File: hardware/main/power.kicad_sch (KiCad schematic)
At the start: 5 parts

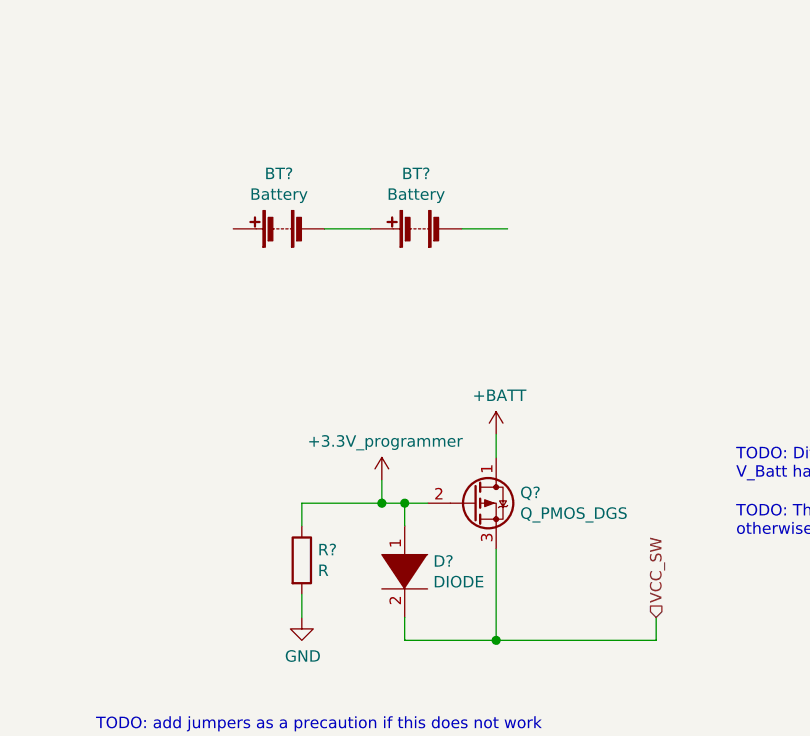
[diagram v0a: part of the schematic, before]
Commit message: Add new board outline
Reason: This makes the first design iteration of the case possible.
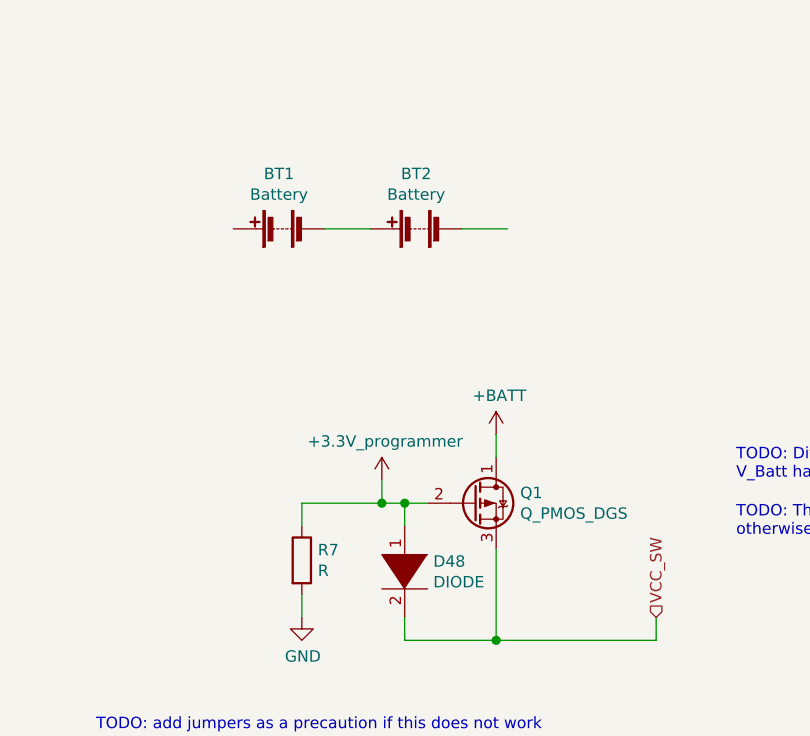
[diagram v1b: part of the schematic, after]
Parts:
- gave numbers to parts that had none: 5
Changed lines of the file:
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@@
   (symbol (lib_id "power:+5V") (at 40.64 34.29 0) (unit 1)
     (in_bom yes) (on_board yes)
-    (property "Reference" "#PWR?" (id 0) (at 40.64 38.1 0)
+    (property "Reference" "#PWR0127" (id 0) (at 40.64 38.1 0)
       (effects (font (size 1.27 1.27)) hide)
     )
@@
   (symbol (lib_id "power:+3.3V") (at 81.28 121.92 0) (unit 1)
     (in_bom yes) (on_board yes)
-    (property "Reference" "#PWR?" (id 0) (at 81.28 125.73 0)
+    (property "Reference" "#PWR0126" (id 0) (at 81.28 125.73 0)
       (effects (font (size 1.27 1.27)) hide)
     )
@@
   (symbol (lib_id "power:+BATT") (at 93.98 116.84 0) (unit 1)
     (in_bom yes) (on_board yes)
-    (property "Reference" "#PWR?" (id 0) (at 93.98 120.65 0)
+    (property "Reference" "#PWR0125" (id 0) (at 93.98 120.65 0)
       (effects (font (size 1.27 1.27)) hide)
     )
@@
   (symbol (lib_id "power:GND") (at 72.39 137.16 0) (unit 1)
     (in_bom yes) (on_board yes)
-    (property "Reference" "#PWR?" (id 0) (at 72.39 143.51 0)
+    (property "Reference" "#PWR0128" (id 0) (at 72.39 143.51 0)
       (effects (font (size 1.27 1.27)) hide)
     )
@@
   (symbol (lib_id "Device:R") (at 72.39 130.81 0) (unit 1)
     (in_bom yes) (on_board yes)
-    (property "Reference" "R?" (id 0) (at 74.1681 129.6606 0)
+    (property "Reference" "R7" (id 0) (at 74.1681 129.6606 0)
       (effects (font (size 1.27 1.27)) (justify left))
     )
@@
   (symbol (lib_id "Device:Battery") (at 69.85 93.98 90) (unit 1)
     (in_bom yes) (on_board yes)
-    (property "Reference" "BT?" (id 0) (at 69.85 87.8648 90))
+    (property "Reference" "BT1" (id 0) (at 69.85 87.8648 90))
     (property "Value" "Battery" (id 1) (at 69.85 90.1635 90))
     (property "Footprint" "" (id 2) (at 68.326 93.98 90)
@@
   (symbol (lib_id "Device:Battery") (at 85.09 93.98 90) (unit 1)
     (in_bom yes) (on_board yes)
-    (property "Reference" "BT?" (id 0) (at 85.09 87.8648 90))
+    (property "Reference" "BT2" (id 0) (at 85.09 87.8648 90))
     (property "Value" "Battery" (id 1) (at 85.09 90.1635 90))
     (property "Footprint" "" (id 2) (at 83.566 93.98 90)
@@
   (symbol (lib_id "pspice:DIODE") (at 83.82 132.08 270) (unit 1)
     (in_bom yes) (on_board yes)
-    (property "Reference" "D?" (id 0) (at 86.9951 130.9306 90)
+    (property "Reference" "D48" (id 0) (at 86.9951 130.9306 90)
       (effects (font (size 1.27 1.27)) (justify left))
     )
@@
   (symbol (lib_id "Device:Q_PMOS_DGS") (at 91.44 124.46 0) (unit 1)
     (in_bom yes) (on_board yes)
-    (property "Reference" "Q?" (id 0) (at 96.6471 123.3106 0)
+    (property "Reference" "Q1" (id 0) (at 96.6471 123.3106 0)
       (effects (font (size 1.27 1.27)) (justify left))
     )

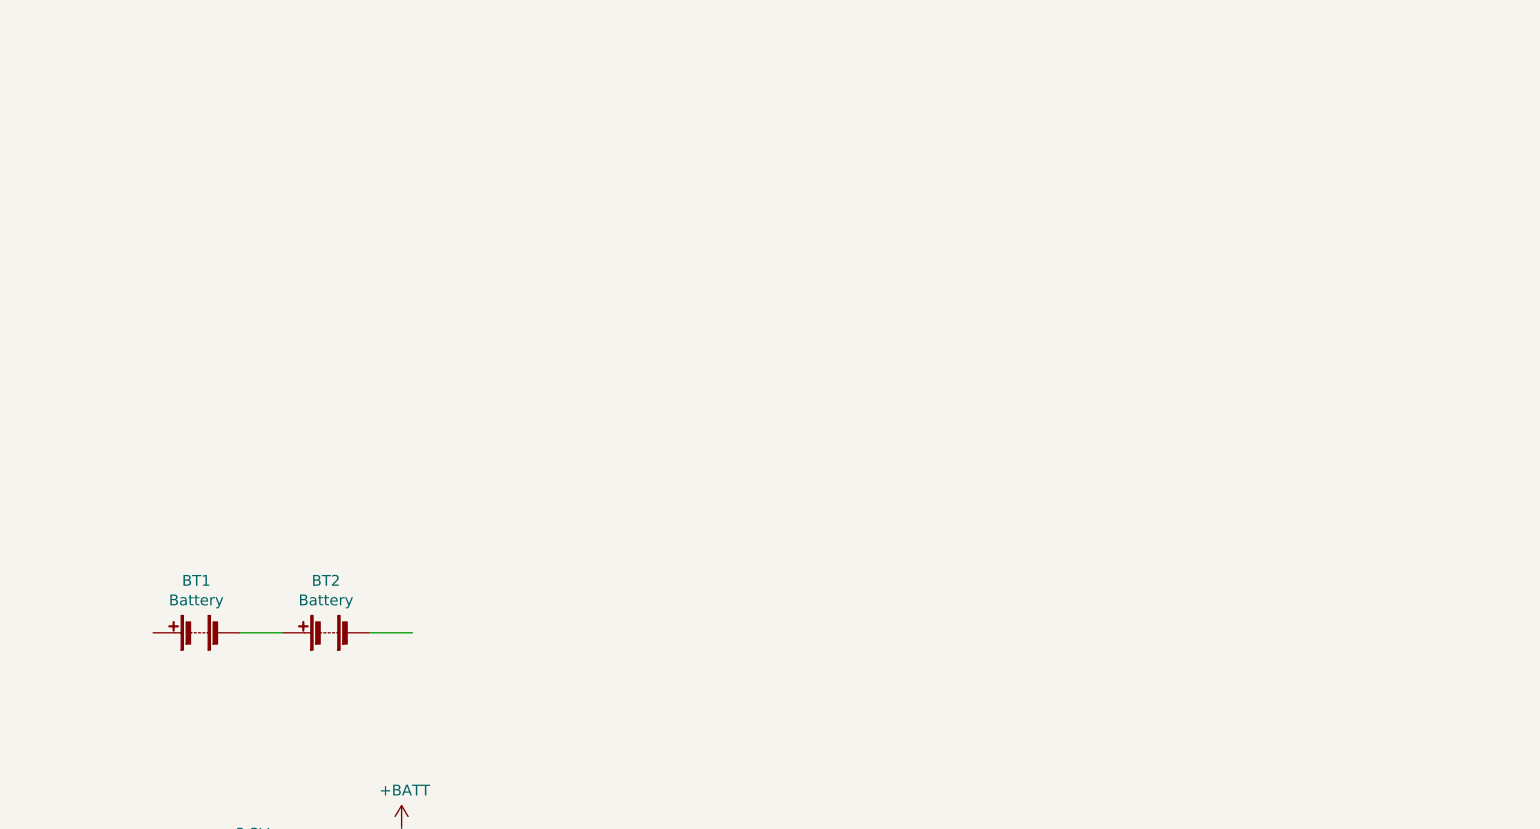
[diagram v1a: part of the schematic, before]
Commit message: Add MCU-controlled battery balancing.
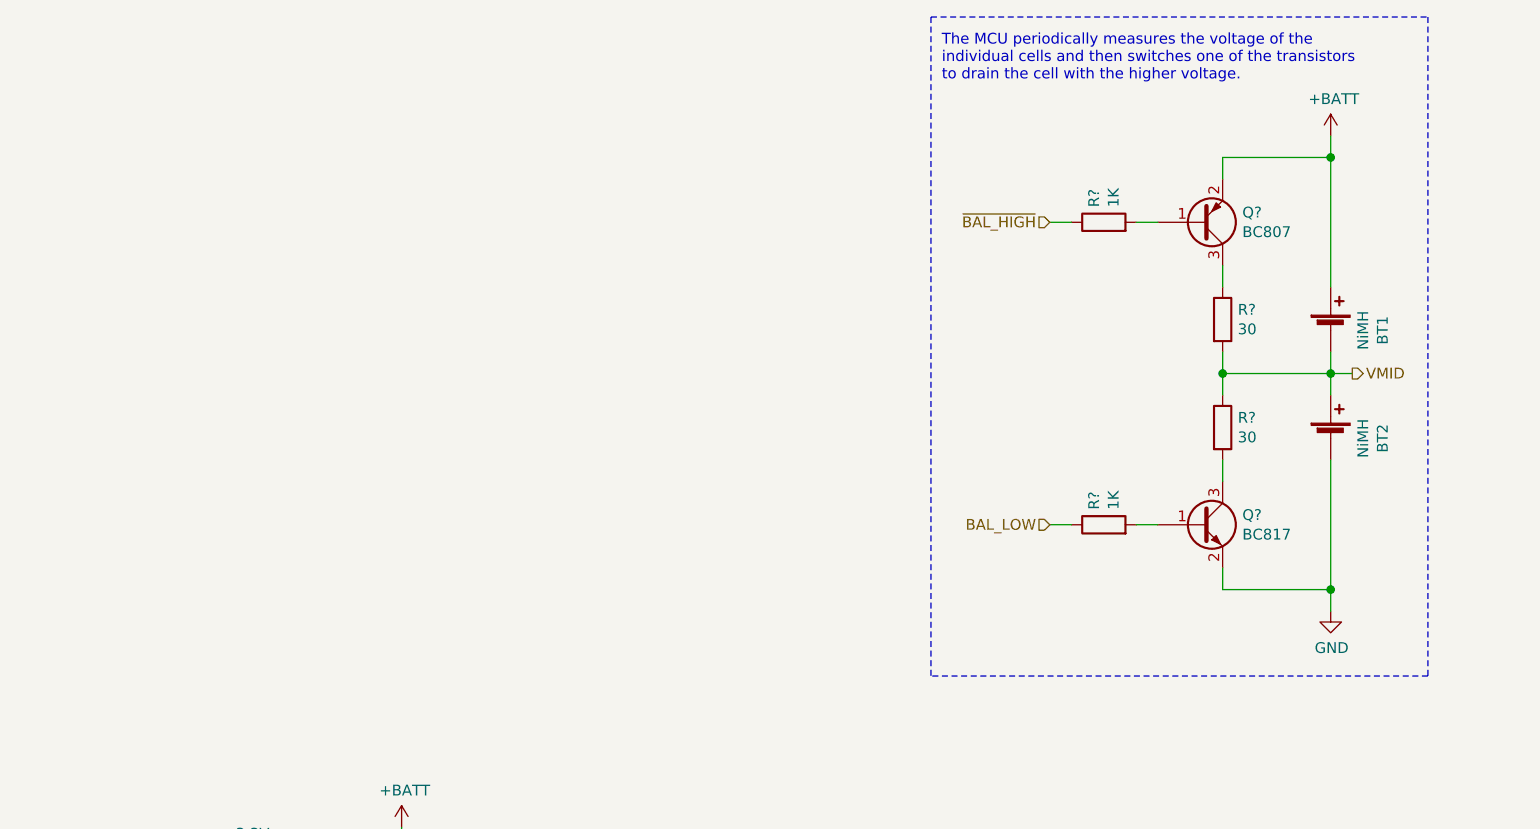
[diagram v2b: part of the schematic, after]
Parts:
- added Q?: BC817, Package_TO_SOT_SMD:SOT-23, symbol Transistor_BJT:BC817
- added Q?: BC807, Package_TO_SOT_SMD:SOT-23, symbol Transistor_BJT:BC807
- added R? (x2): 30, Resistor_SMD:R_0603_1608Metric, symbol Device:R
- added R? (x2): 1K, Resistor_SMD:R_0603_1608Metric, symbol Device:R
- BT1, BT2: value Battery -> NiMH; symbol Device:Battery -> Device:Battery_Cell
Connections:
- net +BATT: now also BT1.1 (+), Q?.2 (E)
- net GND: now also BT2.2 (-), Q?.2 (E)
- net VMID: now reaches BT1.2 (-), BT2.1 (+)
- net VMID: now also R?.1, R?.2
- new net: Q?.3 (C), R?.1
- new net: Q?.3 (C), R?.2
- new net: Q?.1 (B), R?.2 (x2)
- new net BAL_LOW: R?.1
- new net ~BAL_HIGH: R?.1
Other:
- note added: "The MCU periodically measures the voltage of the individual cells and then switches one of the transistors to drain the cell with the higher voltage."

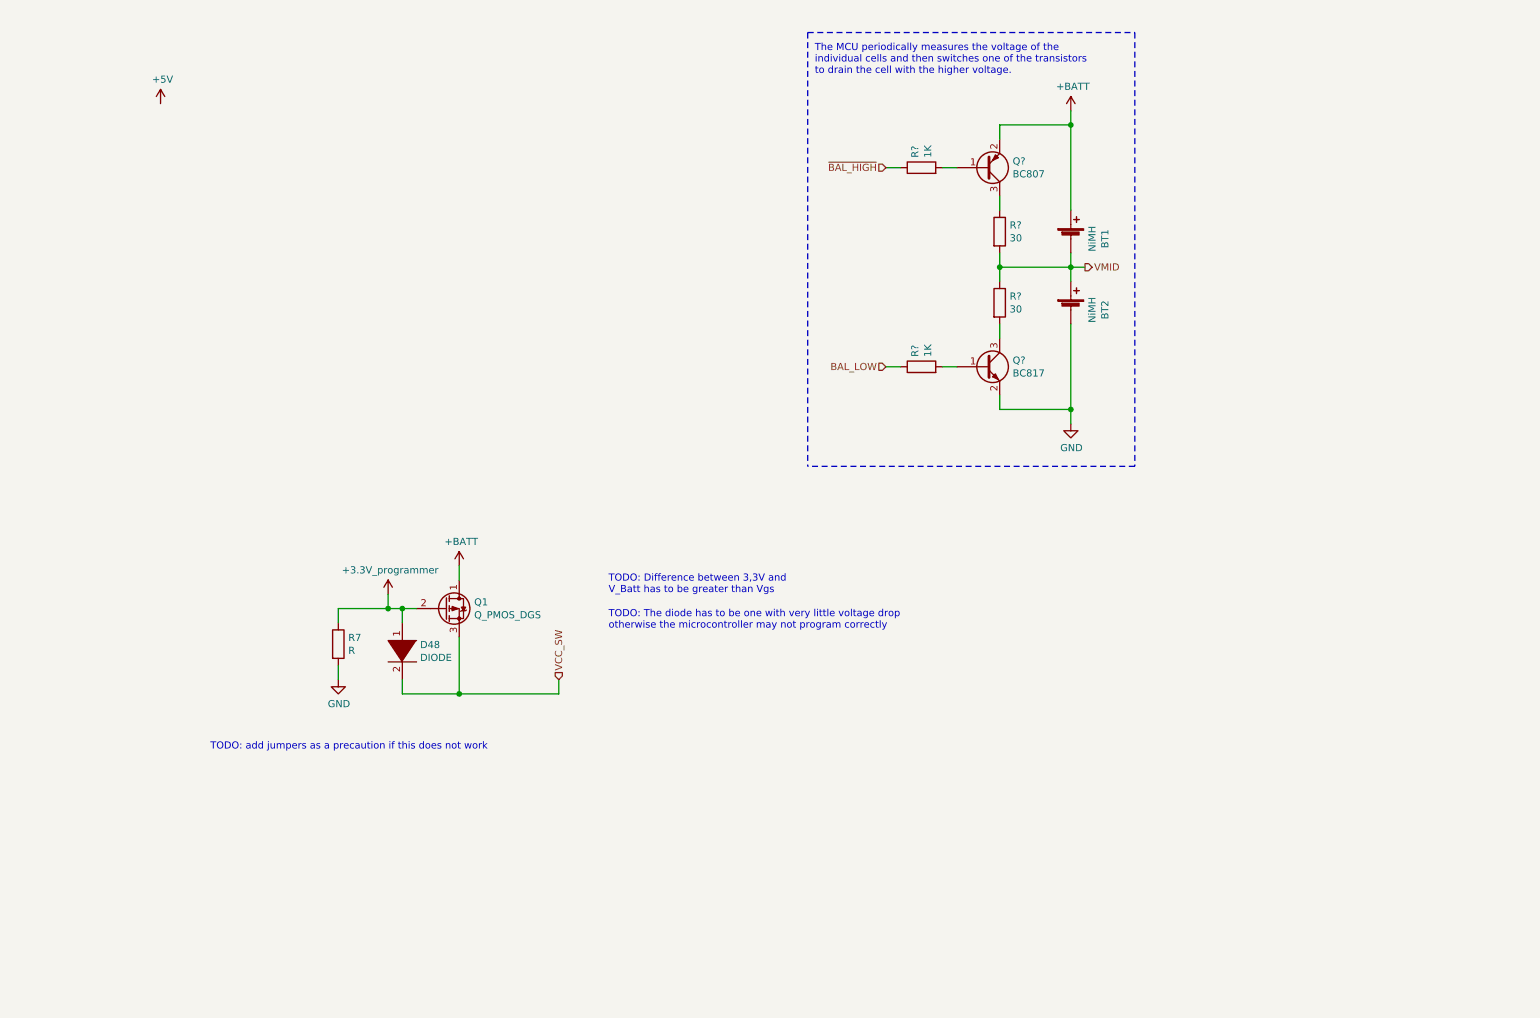
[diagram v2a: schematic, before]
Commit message: Add power supply and battery charging circuitry.
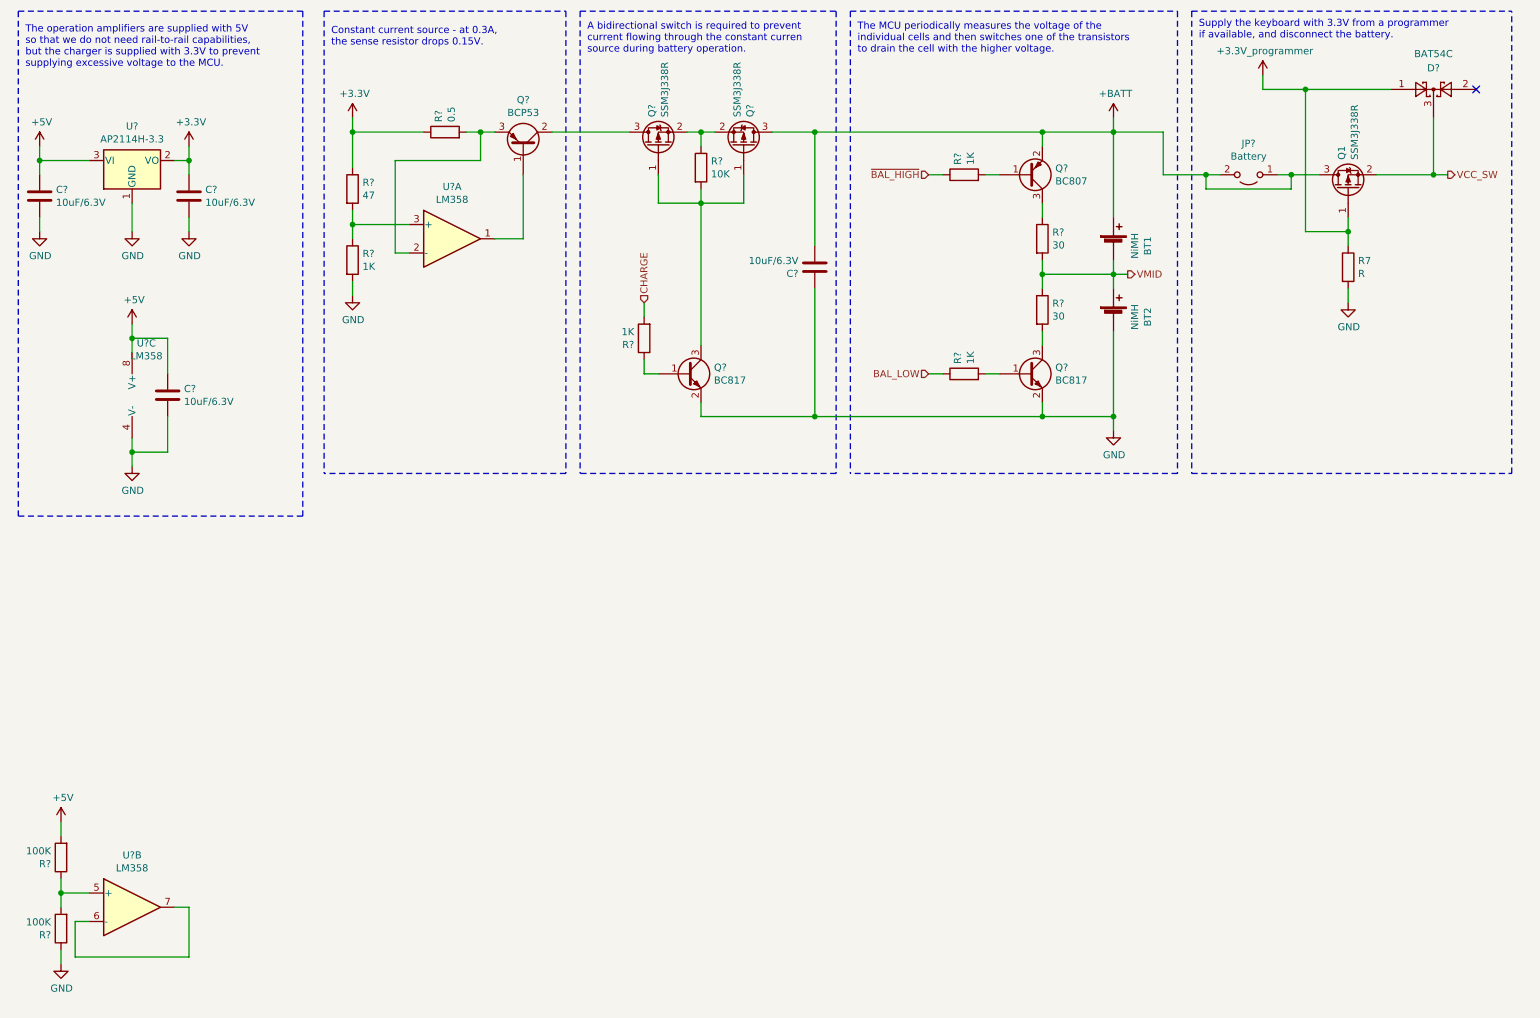
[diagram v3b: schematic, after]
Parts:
- removed D48: DIODE, symbol pspice:DIODE
- added C? (x4): 10uF/6.3V, symbol Device:C
- added D?: BAT54C, Package_TO_SOT_SMD:SOT-23, symbol Diode:BAT54C
- added JP?: Battery, symbol Jumper:Jumper_2_Open
- added Q? (x2): SSM3J338R, Package_TO_SOT_SMD:SOT-23_Handsoldering, symbol Device:Q_PMOS_GSD
- added Q?: BC817, Package_TO_SOT_SMD:SOT-23, symbol Transistor_BJT:BC817
- added Q?: BCP53, Package_TO_SOT_SMD:SOT-223-3_TabPin2, symbol Transistor_BJT:BCP53
- added R? (x2): 100K, Resistor_SMD:R_0603_1608Metric, symbol Device:R
- added R? (x2): 1K, Resistor_SMD:R_0603_1608Metric, symbol Device:R
- added R?: 10K, Resistor_SMD:R_0603_1608Metric, symbol Device:R
- added R?: 47, Resistor_SMD:R_0603_1608Metric, symbol Device:R
- added R?: 0.5, symbol Device:R
- added U? (x3): LM358, symbol Amplifier_Operational:LM358
- added U?: AP2114H-3.3, Package_TO_SOT_SMD:SOT-223-3_TabPin2, symbol Regulator_Linear:AMS1117-3.3
- Q1: value Q_PMOS_DGS -> SSM3J338R; footprint (none) -> Package_TO_SOT_SMD:SOT-23_Handsoldering; symbol Device:Q_PMOS_DGS -> Device:Q_PMOS_GSD; Mouser (none) -> 757-SSM3J338RLF; Part Name (none) -> Toshiba SSM3J338R
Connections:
- net +3V3: now also Q1.1 (G), C?.1, D?.1, R?.1, R?.1, U?.2 (VO); no longer Q1.2 (G)
- net +5V: now also C?.1, C?.1, R?.2, U?.3 (VI), U?.8 (V+)
- net +BATT: now also Q1.3 (D), C?.2, JP?.1 (A), JP?.2 (B), Q?.3 (D); no longer Q1.1 (D)
- net GND: now also C?.1, C?.2, C?.2, C?.2, Q?.2 (E), R?.1, R?.2, U?.1 (GND), U?.4 (V-)
- net VCC_SW: now also Q1.2 (S), D?.3; no longer Q1.3 (S)
- new net: R?.1, R?.2, U?.5 (+)
- new net: Q?.1 (G), Q?.1 (G), Q?.3 (C), R?.2
- new net: Q?.2 (S), Q?.2 (S), R?.1
- new net: U?.6 (-), U?.7
- new net: Q?.1 (B), R?.1
- new net: Q?.2 (C), Q?.3 (D), Q?.4 (C)
- new net: R?.1, R?.2, U?.3 (+)
- new net: Q?.1 (B), U?.1
- new net: Q?.3 (E), R?.2, U?.2 (-)
- new net CHARGE: R?.2
- no-connect marks 0 -> 1
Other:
- note added: "A bidirectional switch is required to prevent current flowing through the constant curren source during battery operation."
- note added: "Constant current source - at 0.3A, the sense resistor drops 0.15V."
- note added: "Supply the keyboard with 3.3V from a programmer if available, and disconnect the battery."
- note added: "The operation amplifiers are supplied with 5V so that we do not need rail-to-rail capabilities, but the charger is supplied with 3.3V to prevent supplying excessive voltage to the MCU."
- note removed: "TODO: Difference between 3,3V and V_Batt has to be greater than Vgs"
- note removed: "TODO: The diode has to be one with very little voltage drop otherwise the microcontroller may not program correctly"
- note removed: "TODO: add jumpers as a precaution if this does not work"
- moved on the sheet: BT1, BT2, Q1, Q?, R7, R?
